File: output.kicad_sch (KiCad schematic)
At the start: 103 parts, among them K1 G6K-2G-Y-TR_DC24_DPDT, K10 G6K-2G-Y-TR_DC24_DPDT, K11 G6K-2G-Y-TR_DC24_DPDT, K12 G6K-2G-Y-TR_DC24_DPDT, K13 G6K-2G-Y-TR_DC24_DPDT, K14 G6K-2G-Y-TR_DC24_DPDT, K15 G6K-2G-Y-TR_DC24_DPDT, K16 G6K-2G-Y-TR_DC24_DPDT, K2 G6K-2G-Y-TR_DC24_DPDT, K3 G6K-2G-Y-TR_DC24_DPDT, K4 G6K-2G-Y-TR_DC24_DPDT, K5 G6K-2G-Y-TR_DC24_DPDT, K6 G6K-2G-Y-TR_DC24_DPDT, K7 G6K-2G-Y-TR_DC24_DPDT, K8 G6K-2G-Y-TR_DC24_DPDT, K9 G6K-2G-Y-TR_DC24_DPDT, U14 ULN2803ADWR, U15 ULN2803ADWR, U5 TPS7B6950QDBVRQ1, U6 TLP290-4(TPE, U7 TLP290-4(TPE, U8 TLP290-4(TPE, U9 TLP290-4(TPE

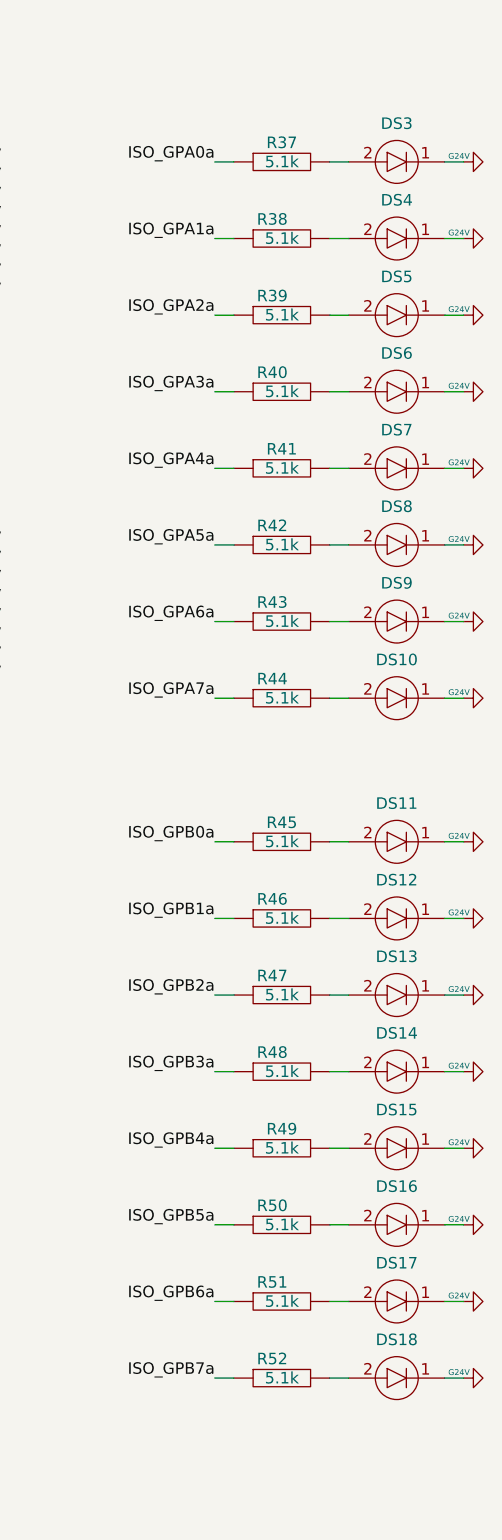
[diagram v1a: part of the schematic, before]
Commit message: assembly updated - dnp led, they should be tight to 24v
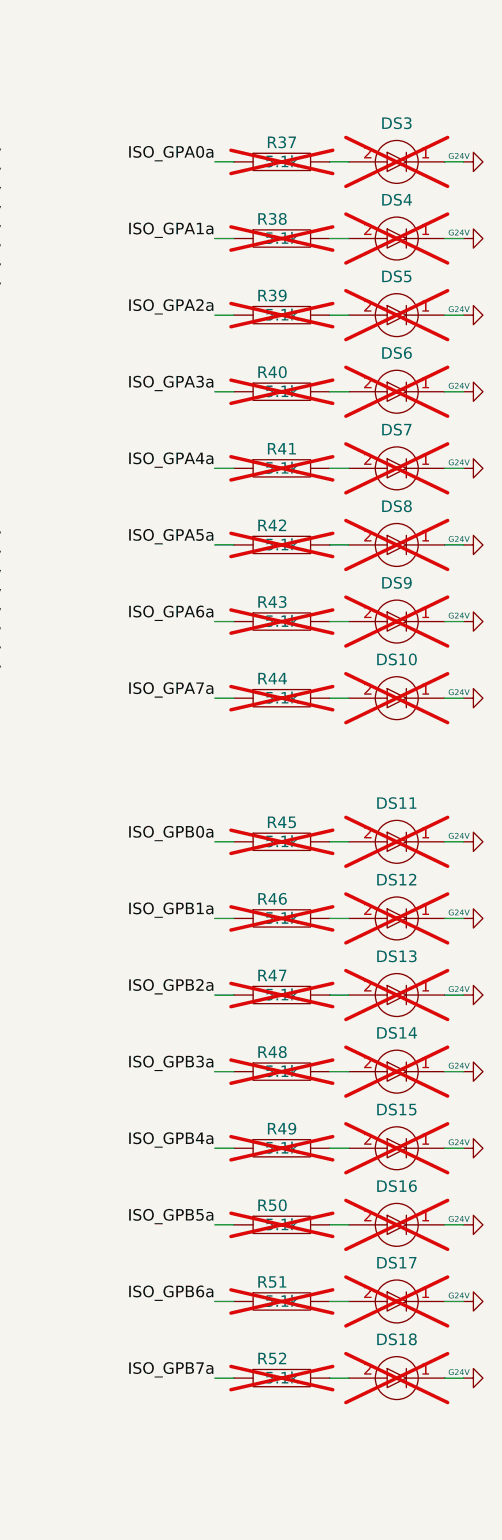
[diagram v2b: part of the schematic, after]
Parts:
- DS10, DS11, DS12, DS13, DS14, DS15, DS16, DS17, DS18, DS3, DS4, DS5, DS6, DS7, DS8, DS9, R37, R38, R39, R40, R41, R42, R43, R44, R45, R46, R47, R48, R49, R50, R51, R52: fit_field (none) -> DNP; now not fitted; now left out of the parts list
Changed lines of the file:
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@@
-(kicad_sch (version 20230409) (generator eeschema)
+(kicad_sch (version 20230620) (generator eeschema)
   (paper "A3")
   (title_block

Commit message: - zero origin on so - silk - sch trig and rtsi lines need 510 resistor - assembly updated - sch and pcb project name and rev - no changes to gerber, old one can be used
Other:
- title: EOL ECU POWER CARD -> EOL ECU MIX CARD
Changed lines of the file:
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@@
   (paper "A3")
   (title_block
-    (title "EOL ECU POWER CARD")
-    (date "2023-04-03")
-    (rev "0B")
+    (title "EOL ECU MIX CARD")
+    (date "2023-09-26")
+    (rev "0C")
     (company "ARXTRON TECHNOLOGIES")
     (comment 1 "A0180-V0")
